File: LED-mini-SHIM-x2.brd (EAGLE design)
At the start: 50.8 x 27.9 mm, 52 parts, among them IC1 TXB0101DCKR, IC2 TXB0101DCKR

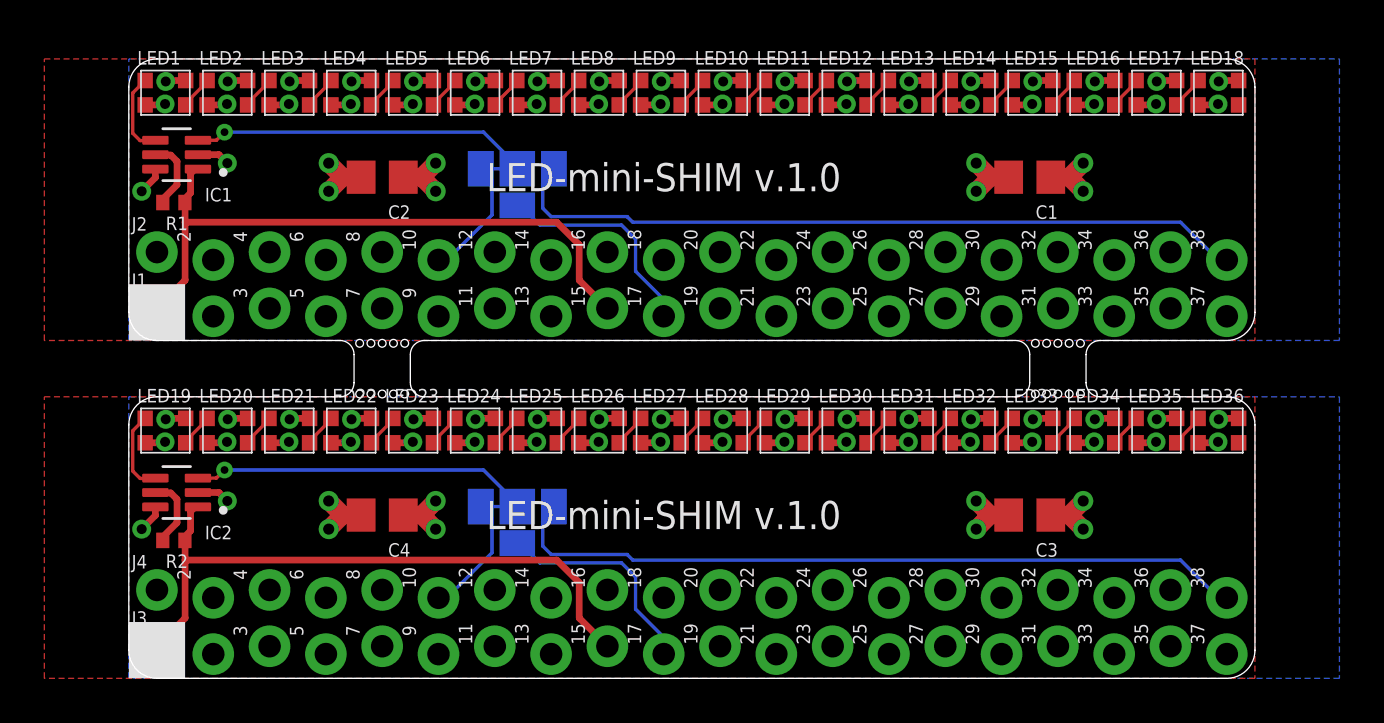
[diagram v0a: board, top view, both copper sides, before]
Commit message: Moved some traces and vias around
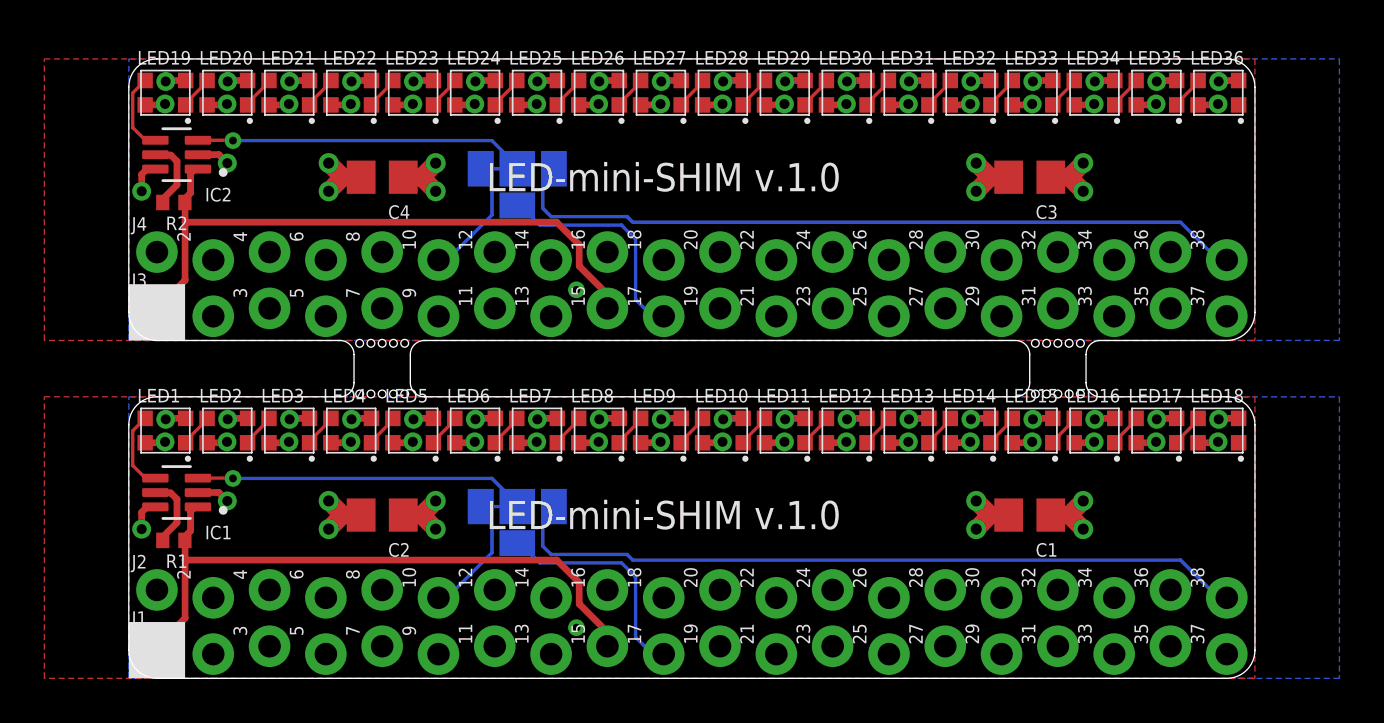
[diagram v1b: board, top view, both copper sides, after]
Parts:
- moved C1 15.2 mm to (40.6, 7.37)
- moved C2 15.2 mm to (11.4, 7.37)
- moved C3 15.2 mm to (40.6, 22.6)
- moved C4 15.2 mm to (11.4, 22.6)
- moved J1 15.2 mm to (1.27, 1.27)
- moved J3 15.2 mm to (1.27, 16.5)
- moved R1 15.2 mm to (2.03, 6.22)
- moved R2 15.2 mm to (2.03, 21.5)
- moved IC1 15.2 mm to (2.16, 8.38)
- moved IC2 15.2 mm to (2.16, 23.6)
- moved J2 15.2 mm to (1.27, 3.81)
- moved J4 15.2 mm to (1.27, 19.1)
- moved LED1 15.2 mm to (1.65, 11.2)
- moved LED10 15.2 mm to (26.8, 11.2)
- moved LED11 15.2 mm to (29.6, 11.2)
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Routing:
- net 5V1: track 23.0 -> 23.2 mm, vias 23 -> 24
- net 5V: track 23.0 -> 23.2 mm, vias 23 -> 24
